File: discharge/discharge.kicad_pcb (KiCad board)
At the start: 2 copper layers, 85 x 75 mm, 15 parts, among them J1 Conn_SDC, J2 Conn_HV_IN, J3 Conn_HV_OUT, K1 5503-12-1

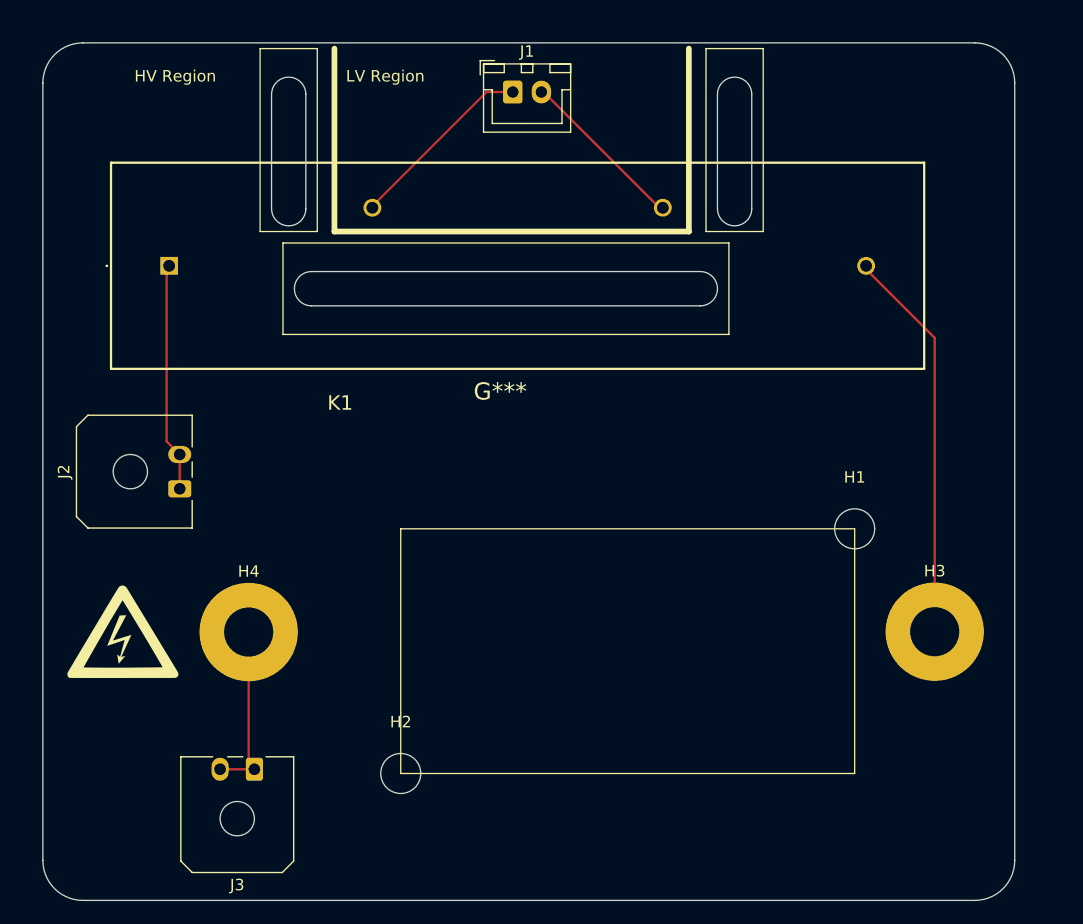
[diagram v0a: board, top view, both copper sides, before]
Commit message: chore: reduce board size and increase trace width
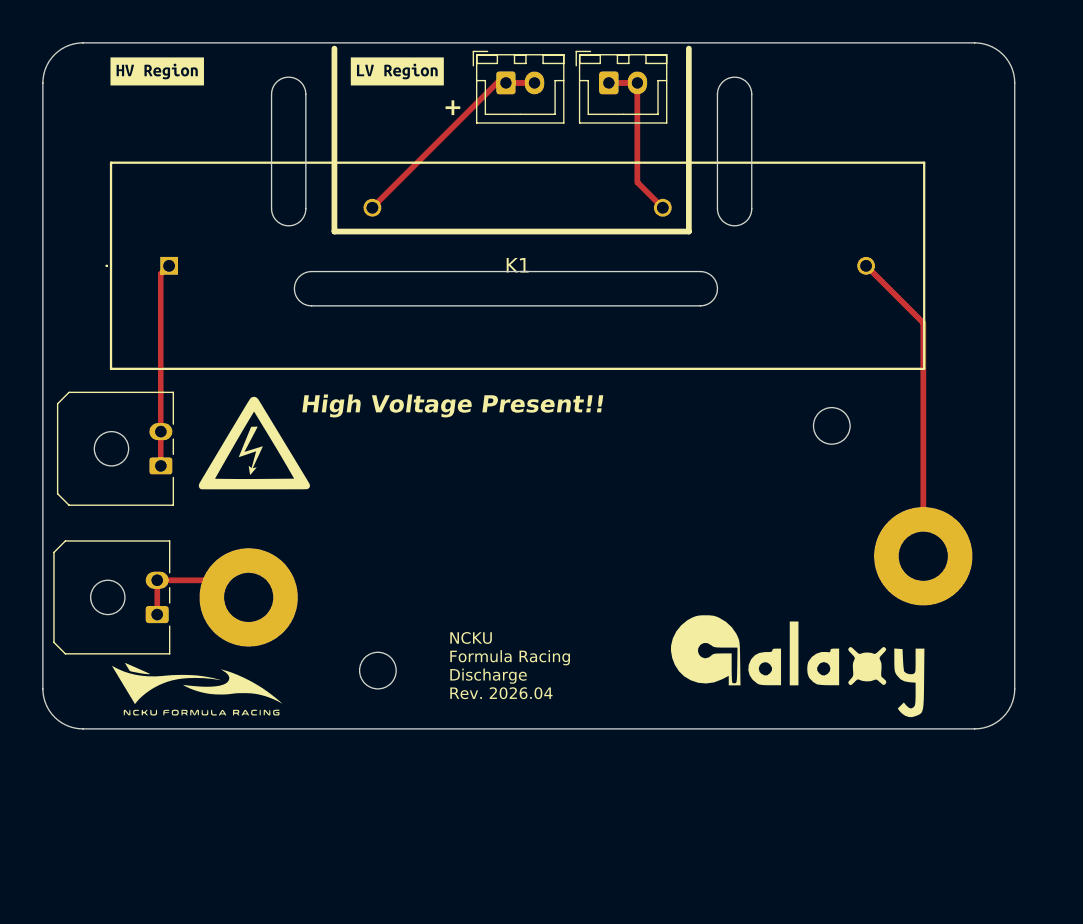
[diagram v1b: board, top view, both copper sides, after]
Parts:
- added J4: GND, Connector_JST:JST_XH_B2B-XH-A_1x02_P2.50mm_Vertical, F.Cu at (140.5, 74.0)
- added kibuzzard-69D15BD9: G***, kibuzzard-69D15BD9, F.Cu at (122.0, 73.0)
- added kibuzzard-69D15BE3: G***, kibuzzard-69D15BE3, F.Cu at (101.0, 73.0)
- G*** (x2): moved to F.Cu
- H1, H2: value R_Pad -> MountingHole; footprint MountingHole:MountingHole_3.5mm -> MountingHole:MountingHole_3.2mm_M3
- K1: footprint Library:5503121 -> 5503-12-1:5503121
- moved G*** 43.1 mm to (104.5, 127.0), turned to 0 degrees
- moved G*** 35.4 mm to (157.0, 125.0), turned to 0 degrees
- moved G*** 30.7 mm to (141.0, 109.5)
- moved G*** 20.1 mm to (109.5, 105.5)
- moved J3 16.0 mm to (101.0, 120.5), turned to 90 degrees
- moved G*** 9.22 mm to (154.5, 122.0)
- moved H1 9.22 mm to (160.0, 104.0)
- moved H2 9.22 mm to (120.3, 125.4)
- moved H3 6.68 mm to (168.0, 115.4)
- moved H4 3.03 mm to (109.0, 119.0)
- moved J2 2.59 mm to (101.3, 107.5)
- moved J1 1.00 mm to (131.5, 74.0)
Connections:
- J1 pad 1: VDC -> Net-(J1-Pin_1)
- J1 pad 2: GND -> Net-(J1-Pin_1)
- K1 pad 2: VDC -> Net-(J1-Pin_1)
- K1 pad 3: GND -> Net-(J4-Pin_1)
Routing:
- net Net-(J1-Pin_1): track 0.00 -> 18.7 mm
- net VDC: track 16.7 -> 0.00 mm
- net GND: track 14.6 -> 0.00 mm
- net Net-(J4-Pin_1): track 0.00 -> 14.3 mm
- net Net-(H3-Pad1): track 34.5 -> 27.5 mm
- net Net-(J3-Pin_1): track 15.2 -> 11.6 mm
- net Net-(J2-Pin_1): track 19.9 -> 17.8 mm
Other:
- board size 85 x 75 mm -> 85 x 60 mm
- board text added: "+"
- board text added: "High Voltage Present!!"
- board text removed: "HV Region"
- board text removed: "LV Region"

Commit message: feat: combine 2 disC into PCB
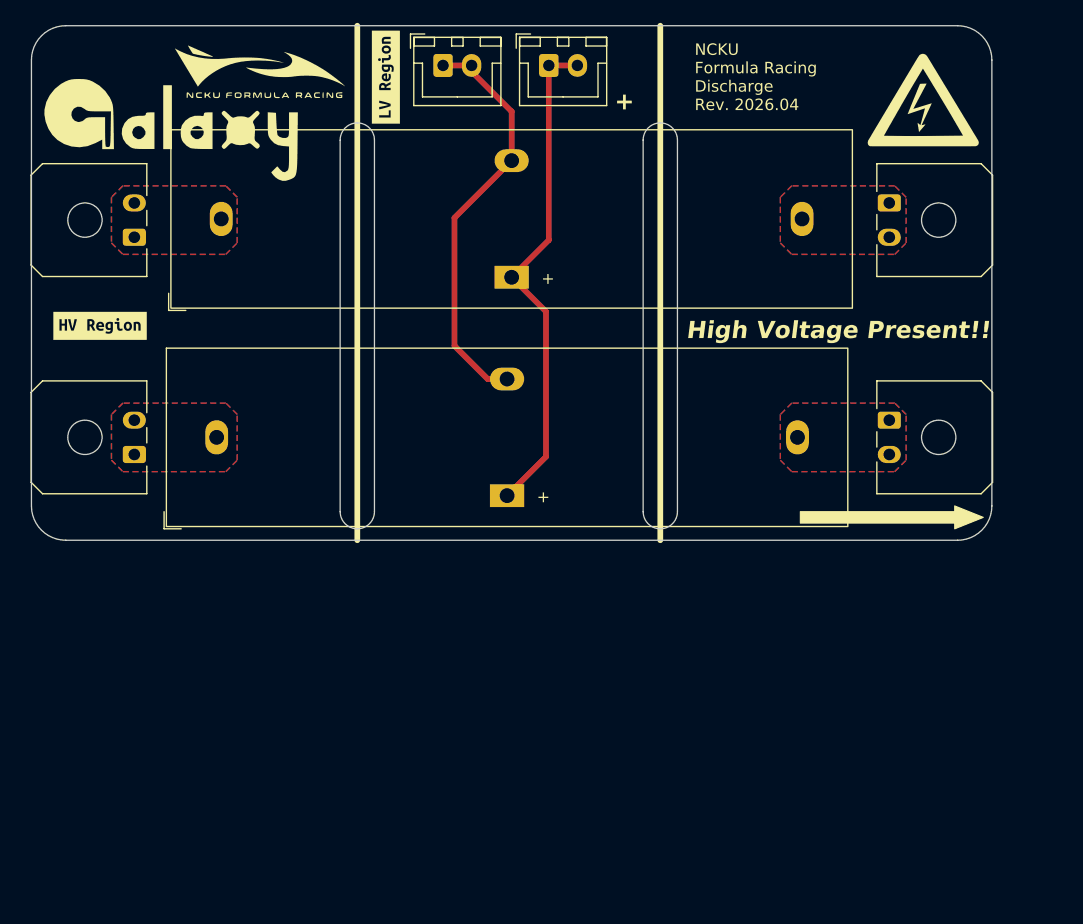
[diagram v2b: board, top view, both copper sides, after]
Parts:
- removed the G*** at (141.0, 109.5)
- removed H1, H2: MountingHole, MountingHole:MountingHole_3.2mm_M3
- removed H3, H4: R_Pad, MountingHole:MountingHole_4.3mm_M4_Pad
- added J5: Conn_HV_IN, Connector_Molex:Molex_Micro-Fit_3.0_43650-0200_1x02_P3.00mm_Horizontal, F.Cu at (165.0, 103.5)
- added J6: Conn_HV_OUT, Connector_Molex:Molex_Micro-Fit_3.0_43650-0200_1x02_P3.00mm_Horizontal, F.Cu at (99.0, 106.5)
- added K2: Relay_SPST-NC, Reed:Reed, F.Cu at (131.6, 105.0)
- K1: value 5503-12-1 -> Relay_SPST-NC; footprint 5503-12-1:5503121 -> Reed:Reed
- moved G*** 72.1 mm to (102.2, 78.1)
- moved J2 67.7 mm to (165.0, 84.5), turned to -90 degrees
- moved G*** 65.7 mm to (168.0, 75.5)
- moved G*** 54.3 mm to (110.0, 73.0)
- moved G*** 33.1 mm to (131.5, 90.8)
- moved kibuzzard-6788E0FE 33.1 mm to (131.5, 102.0)
- moved J3 33.1 mm to (99.0, 87.5)
- moved K1 30.2 mm to (132.0, 85.9)
- moved kibuzzard-69D15BE3 22.8 mm to (96.0, 95.2)
- moved J4 14.6 mm to (126.0, 72.5)
- moved J1 4.05 mm to (135.2, 72.5)
- moved G*** 1.80 mm to (153.5, 120.5)
- moved kibuzzard-69D15BD9 1.12 mm to (121.0, 73.5), turned to 90 degrees
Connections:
- J1 pad 1: Net-(J1-Pin_1) -> VDC
- J1 pad 2: Net-(J1-Pin_1) -> VDC
- J4 pad 1: Net-(J4-Pin_1) -> GND
- J4 pad 2: Net-(J4-Pin_1) -> GND
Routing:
- net VDC: track 0.00 -> 44.1 mm
- net GND: track 0.00 -> 36.3 mm
- net Net-(H3-Pad1): track 27.5 -> 0.00 mm
- net Net-(J1-Pin_1): track 18.7 -> 0.00 mm
- net Net-(J2-Pin_1): track 17.8 -> 0.00 mm
- net Net-(J4-Pin_1): track 14.3 -> 0.00 mm
- net Net-(J3-Pin_1): track 11.6 -> 0.00 mm
- added copper zone on B.Cu, net Net-(J2-Pin_1)
- added copper zone on F.Cu, net Net-(J2-Pin_1)
- added copper zone on B.Cu, net Net-(J3-Pin_1)
- added copper zone on F.Cu, net Net-(J3-Pin_1)
- added copper zone on B.Cu, net Net-(J5-Pin_1)
- added copper zone on F.Cu, net Net-(J5-Pin_1)
- added copper zone on B.Cu, net Net-(J6-Pin_1)
- added copper zone on F.Cu, net Net-(J6-Pin_1)
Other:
- board size 85 x 60 mm -> 84 x 45 mm

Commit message: finish timer layout
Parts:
- added C1: 100n, Capacitor_SMD:C_0603_1608Metric, F.Cu at (116.7, 120.0)
- added C2: 100u, Capacitor_SMD:C_0603_1608Metric, F.Cu at (103.3, 121.0)
- added C3: 100n, Capacitor_SMD:C_0603_1608Metric, F.Cu at (115.0, 126.2)
- added C4: 100n, Capacitor_SMD:C_0603_1608Metric, F.Cu at (118.0, 126.2)
- added C5: 1u, Capacitor_SMD:C_0603_1608Metric, F.Cu at (132.0, 125.8)
- added C6: 1u, Capacitor_SMD:C_0603_1608Metric, F.Cu at (109.2, 127.5)
- added D1: D_Small, Diode_SMD:D_SOD-123F, F.Cu at (136.0, 125.6)
- added J7: Conn, Connector_JST:JST_XH_B2B-XH-A_1x02_P2.50mm_Vertical, F.Cu at (170.5, 121.5)
- added K3: JY-12H-K, JY12Hk:JY12HK, F.Cu at (142.0, 120.2)
- added Q2: Si2301CDS, Package_TO_SOT_SMD:SOT-23, F.Cu at (134.0, 120.5)
- added R1: 4.7k, Resistor_SMD:R_0603_1608Metric, F.Cu at (103.5, 123.8)
- added R2: 68k, Resistor_SMD:R_0603_1608Metric, F.Cu at (103.5, 127.3)
- added R4: 10k, Resistor_SMD:R_0603_1608Metric, F.Cu at (128.3, 120.2)
- added R5: 10k, Resistor_SMD:R_0603_1608Metric, F.Cu at (116.8, 122.0)
- added U1: SE555D, Package_SO:SOIC-8_3.9x4.9mm_P1.27mm, F.Cu at (109.5, 122.5)
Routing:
- net GND: track 36.3 -> 162.2 mm
- net VDC: track 44.1 -> 111.5 mm
- net Timer: track 0.00 -> 23.3 mm, vias 0 -> 2
- net Net-(J7-Pin_2): track 0.00 -> 19.9 mm
- net Net-(J7-Pin_1): track 0.00 -> 13.3 mm
- net Net-(U1-TR): track 0.00 -> 11.8 mm
- net Net-(U1-DIS): track 0.00 -> 10.4 mm
- net Net-(U1-CV): track 0.00 -> 9.59 mm
- net Net-(R1-Pad1): track 0.00 -> 1.85 mm
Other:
- board size 84 x 45 mm -> 84 x 62 mm

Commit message: modify discharge ver2
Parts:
- removed C3, C4: 100n, Capacitor_SMD:C_0603_1608Metric
- removed C5: 1u, Capacitor_SMD:C_0603_1608Metric
- removed Q2: Si2301CDS, Package_TO_SOT_SMD:SOT-23
- removed R5: 10k, Resistor_SMD:R_0603_1608Metric
- added Q1: Si2301CDS, Package_TO_SOT_SMD:SOT-23, F.Cu at (118.5, 123.2)
- C2: value 100u -> 22u; footprint Capacitor_SMD:C_0603_1608Metric -> Capacitor_SMD:C_0805_2012Metric
- D1: value D_Small -> 1N4148W-7-F
- R1: value 4.7k -> 47k
- R2: value 68k -> 280k
- moved C2 34.0 mm to (137.2, 123.6), turned to 90 degrees
- moved R1 28.6 mm to (131.7, 128.3), turned to 0 degrees
- moved C6 26.2 mm to (134.2, 119.8)
- moved R2 24.2 mm to (127.7, 128.3), turned to 0 degrees
- moved U1 18.5 mm to (128.0, 122.9), turned to 0 degrees
- moved C1 17.2 mm to (133.5, 123.6), turned to 90 degrees
- moved D1 16.4 mm to (122.1, 116.8), turned to 0 degrees
- moved R4 9.57 mm to (122.7, 127.9), turned to 90 degrees
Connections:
- C2 pad 1: Net-(U1-DIS) -> Net-(U1-THR)
- D1 pad 1: VDC -> Net-(D1-K)
- K3 pad 9: GND -> Net-(D1-K)
- R1 pad 2: Net-(U1-DIS) -> Net-(U1-THR)
- R4 pad 1: +12V -> VDC
- U1 pad 2: Net-(U1-TR) -> GND
- U1 pad 6: Net-(U1-DIS) -> Net-(U1-THR)
- U1 pad 7: Net-(U1-DIS) -> GND
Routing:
- net GND: track 162.2 -> 86.4 mm
- net Net-(D1-K): track 0.00 -> 34.3 mm, vias 0 -> 4
- net VDC: track 111.5 -> 88.8 mm, vias 0 -> 2
- net Net-(U1-THR): track 0.00 -> 16.1 mm
- net Net-(U1-TR): track 11.8 -> 0.00 mm
- net Timer: track 23.3 -> 12.4 mm, vias 2 -> 0
- net Net-(U1-DIS): track 10.4 -> 0.00 mm
- net Net-(U1-CV): track 9.59 -> 3.21 mm
- net Net-(R1-Pad1): track 1.85 -> 2.35 mm
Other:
- board text added: "NCKU Formula Racing Discharge Rev. 2026.05"
- board text removed: "NCKU Formula Racing Discharge Rev. 2026.04"

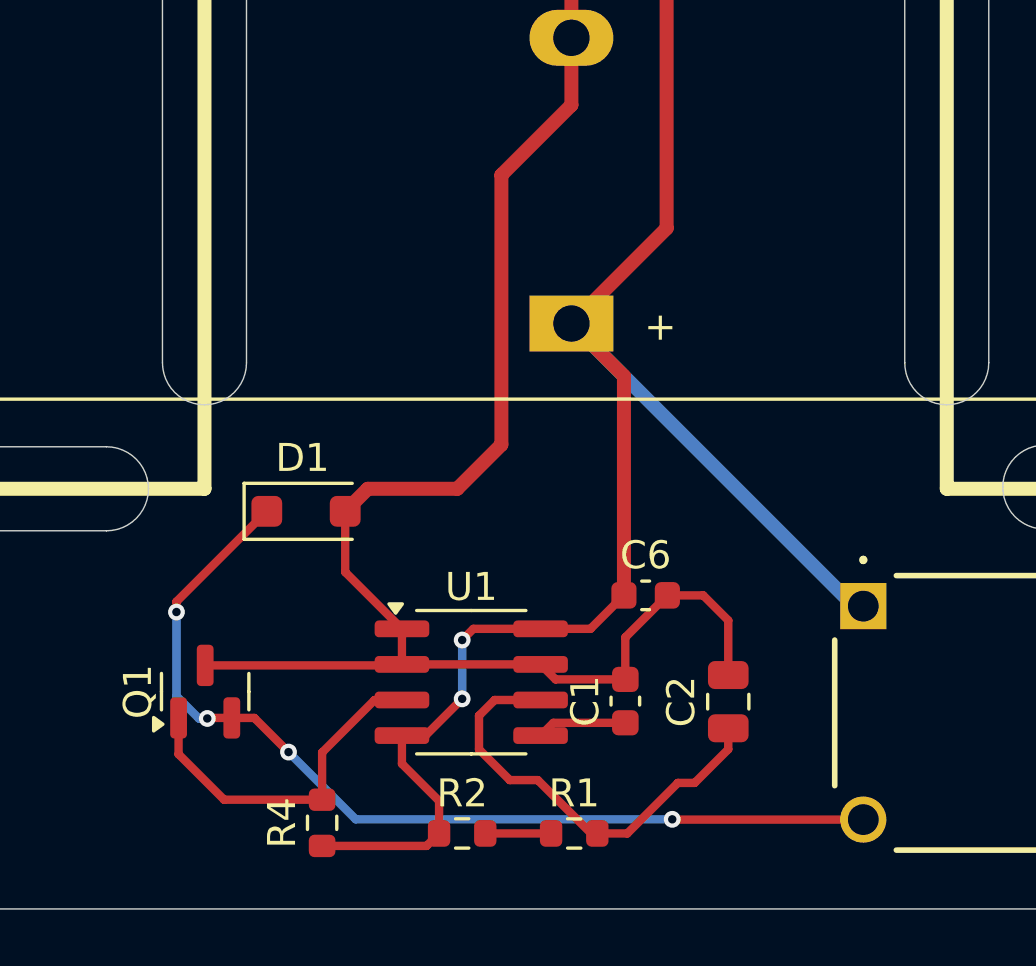
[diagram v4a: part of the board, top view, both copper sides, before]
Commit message: fix: move flyback diode position
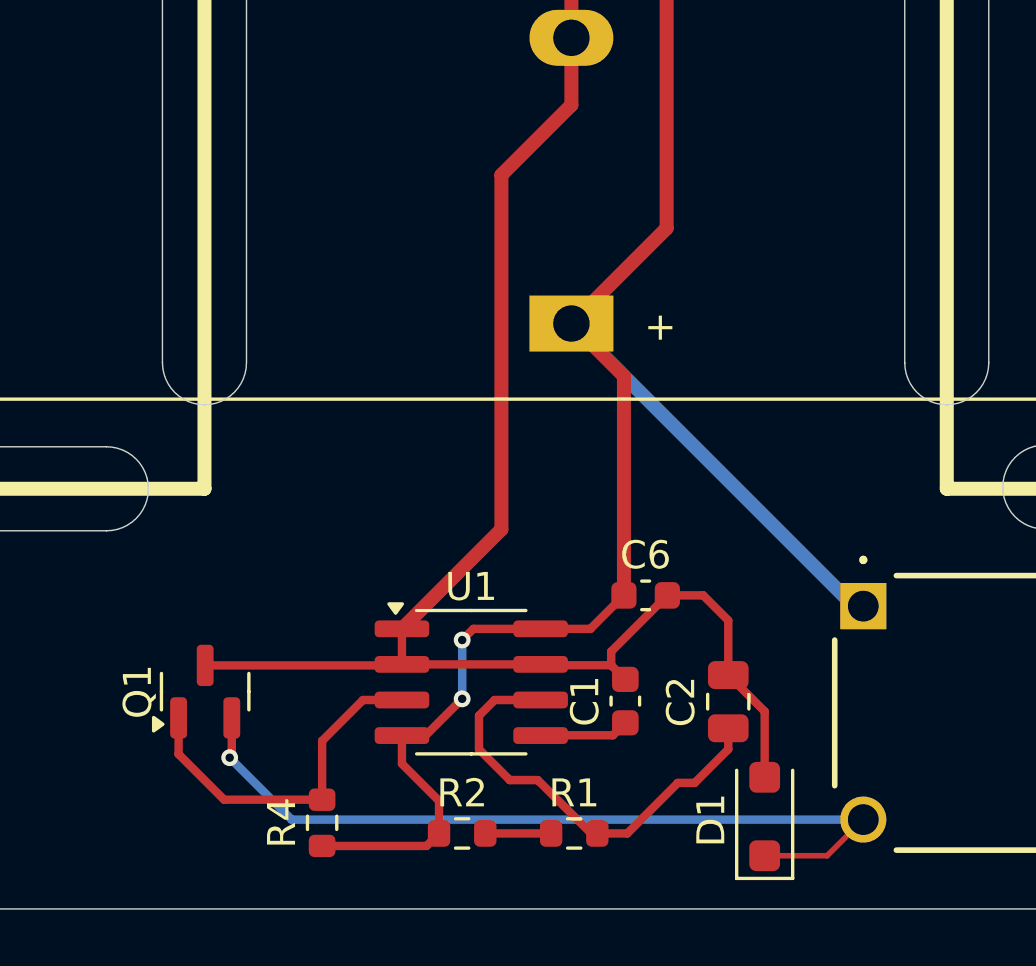
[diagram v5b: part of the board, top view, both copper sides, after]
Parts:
- moved D1 19.7 mm to (138.5, 127.7), turned to 90 degrees
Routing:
- net Net-(D1-K): track 34.3 -> 29.0 mm, vias 4 -> 1
